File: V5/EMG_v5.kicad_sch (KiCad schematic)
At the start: 1 part, among them U501 DSTK22807_ESP32H2_SuperMini_M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

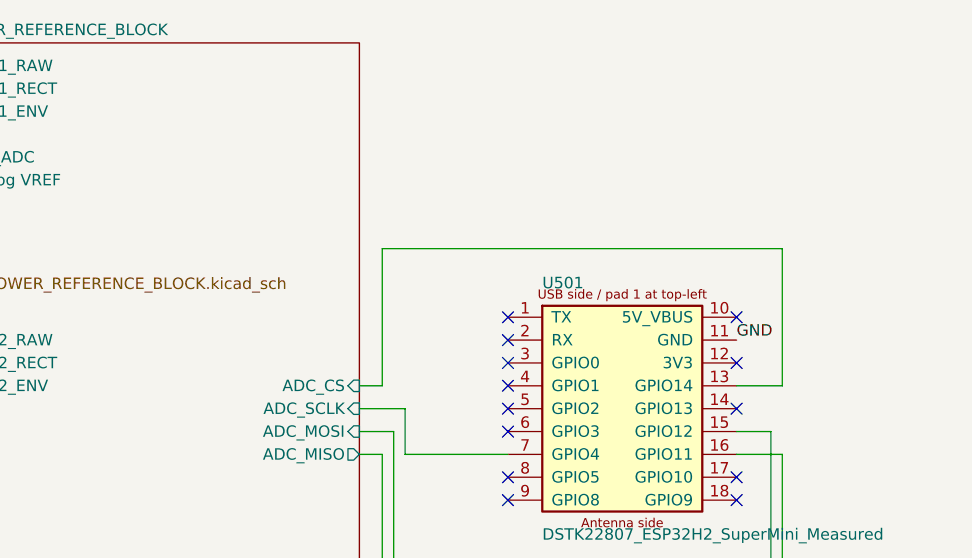
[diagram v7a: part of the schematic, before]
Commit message: add battery powered carrier supply path
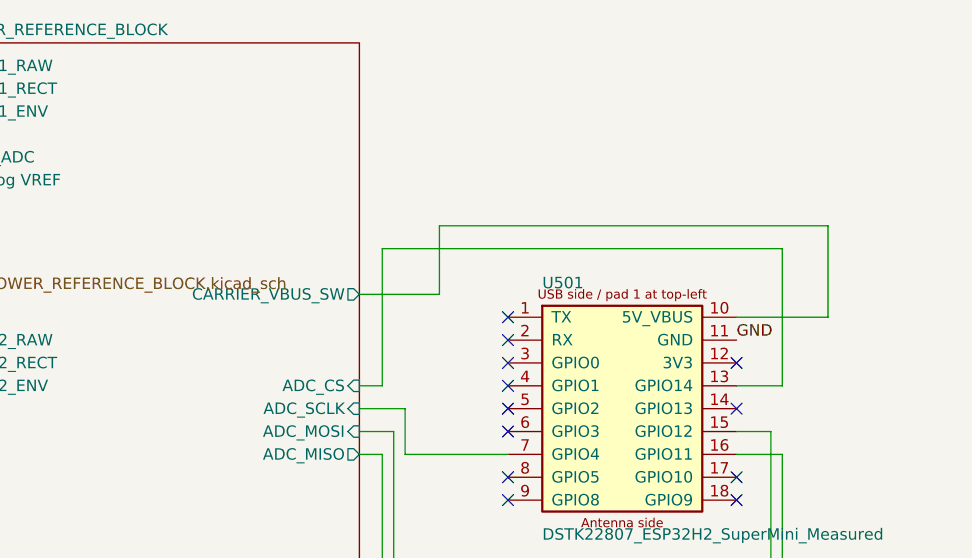
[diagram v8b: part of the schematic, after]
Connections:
- net POWER_REFERENCE_BLOCK/CARRIER_VBUS_SW: now reaches U501.10 (5V_VBUS)
- no-connect marks 13 -> 12
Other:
- sheet POWER_REFERENCE_BLOCK ports: added CARRIER_VBUS_SW; removed none
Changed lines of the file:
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@@
-	)
-	(no_connect
-		(at 210.82 54.61)
 	)
 	(no_connect
@@
 	(no_connect
 		(at 210.82 74.93)
+	)
+	(wire
+		(pts
+			(xy 168.91 52.07) (xy 177.8 52.07)
+		)
+		(stroke
+			(width 0)
+			(type default)
+		)
+	)
+	(wire
+		(pts
+			(xy 177.8 52.07) (xy 177.8 44.45)
+		)
+		(stroke (width 0) (type default))
+	)
+	(wire
+		(pts
+			(xy 177.8 44.45) (xy 220.98 44.45)
+		)
+		(stroke (width 0) (type default))
+	)
+	(wire
+		(pts
+			(xy 220.98 44.45) (xy 220.98 54.61)
+		)
+		(stroke (width 0) (type default))
+	)
+	(wire
+		(pts
+			(xy 220.98 54.61) (xy 210.82 54.61)
+		)
+		(stroke (width 0) (type default))
 	)
 	(wire
@@
 			)
 		)
+		(pin "CARRIER_VBUS_SW" output
+			(at 168.91 52.07 0)
+			(effects
+				(font (size 1.27 1.27))
+				(justify right)
+			)
+		)
